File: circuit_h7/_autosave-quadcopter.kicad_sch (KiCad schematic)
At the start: 143 parts, among them J1 Conn_01x01_Female, J10 Conn_01x01_Female, J11 Conn_01x04_Male, J12 Conn_01x04_Male, J13 Conn_01x01_Female, J14 Conn_01x01_Female, J15 Conn_01x01_Female, J16 Conn_01x01_Female, J17 Conn_01x01_Female, J18 USB_C_Receptacle_USB2.0, J19 Conn_01x08_Male, J2 Conn_01x01_Female, J20 Conn_01x01_Female, J21 Conn_01x01_Female, J22 Conn_01x01_Female, J23 Conn_01x01_Female, J24 Conn_01x01_Female, J25 Conn_01x01_Female, J26 Conn_01x01_Female, J28 Conn_01x01_Female, J29 Conn_01x01_Female, J3 Conn_01x01_Female, J30 Conn_01x01_Female, J31 Conn_01x01_Female, J32 Conn_01x01_Female, J33 Conn_01x01_Female, J37 Conn_01x01_Female, J4 Conn_01x01_Female, J40 Conn_01x01_Female, J41 Conn_01x01_Female, J42 Conn_01x01_Female, J43 Conn_01x01_Female, J44 Conn_01x01_Female, J45 Conn_01x01_Female, J47 Conn_01x01_Female, J48 Conn_01x01_Female, J49 Conn_01x01_Female, J5 Conn_Coaxial, J50 Conn_01x01_Female, J6 Conn_01x06_Male, J7 Conn_01x01_Female, J8 Conn_01x01_Female, J9 Conn_01x01_Female, Q1 AO3400A, SW1 SW_DIP_x01, U1 STM32H723VGH6, U10 ESP8285, U11 AMS1117-5.0, U12 TPS5430DDA, U13 5v, 3A, U2 ICM-42605, U3 DPS310, U4 3V3, U5 EUP3458 1.2A, 30V max input, 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, U6 2450FM07D0034T, U7 W25Q80DVUXIE TR (16M), U8 SX1281, U9 5v, 500mA, Y1 16M, Y2 52Mhz, 12pF, Y3 40M

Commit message: More work on H7 board. Removed ctrl mix from firmware
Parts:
- added J27, J34, J35, J36: Conn_01x01_Female, TestPoint:TestPoint_Pad_1.0x1.0mm, symbol Connector:Conn_01x01_Female
- J12: now left out of the parts list
- J3, J31, J37: footprint TestPoint:TestPoint_Pad_1.5x1.5mm -> TestPoint:TestPoint_Pad_2.0x2.0mm
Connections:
- net GND: now also J27.1 (Pin_1); no longer J12.1 (Pin_1)
- net NRST: now also J36.1 (Pin_1); no longer J12.4 (Pin_4)
- net SWCLK: now also J35.1 (Pin_1); no longer J12.3 (Pin_3)
- net SWDIO: now also J34.1 (Pin_1); no longer J12.2 (Pin_2)
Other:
- moved on the sheet: J12
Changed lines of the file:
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@@
     (effects (font (size 1.27 1.27)) (justify left bottom))
   )
+  (label "NRST" (at 534.67 80.01 180)
+    (effects (font (size 1.27 1.27)) (justify right bottom))
+  )
   (label "M4" (at 427.99 40.64 180)
     (effects (font (size 1.27 1.27)) (justify right bottom))
@@
     (effects (font (size 1.27 1.27)) (justify left bottom))
   )
+  (label "SWDIO" (at 534.67 69.85 180)
+    (effects (font (size 1.27 1.27)) (justify right bottom))
+  )
   (label "ELRS_BUSY" (at 48.26 297.18 180)
     (effects (font (size 1.27 1.27)) (justify right bottom))
@@
     (effects (font (size 1.27 1.27)) (justify right bottom))
   )
+  (label "SWCLK" (at 534.67 74.93 180)
+    (effects (font (size 1.27 1.27)) (justify right bottom))
+  )
   (label "UART1_RX" (at 381 215.9 180)
     (effects (font (size 1.27 1.27)) (justify right bottom))
@@
     (pin "9")
   )
-  (symbol (lib_id "Connector:Conn_01x04_Male") (at 523.24 54.61 0) (unit 1)
-    (in_bom yes) (on_board yes) (fields_autoplaced)
-    (property "Reference" "J12" (id 0) (at 523.875 46.99 0))
-    (property "Value" "Conn_01x04_Male" (id 1) (at 523.875 49.53 0))
-    (property "Footprint" "Anyleaf_Shared:JST PH staggered for 1x04 2mm" (id 2) (at 523.24 54.61 0)
+  (symbol (lib_id "Connector:Conn_01x04_Male") (at 547.37 53.34 0) (unit 1)
+    (in_bom no) (on_board no) (fields_autoplaced)
+    (property "Reference" "J12" (id 0) (at 548.005 45.72 0))
+    (property "Value" "Conn_01x04_Male" (id 1) (at 548.005 48.26 0))
+    (property "Footprint" "Anyleaf_Shared:JST PH staggered for 1x04 2mm" (id 2) (at 547.37 53.34 0)
       (effects (font (size 1.27 1.27)) hide)
     )
-    (property "Datasheet" "~" (id 3) (at 523.24 54.61 0)
+    (property "Datasheet" "~" (id 3) (at 547.37 53.34 0)
       (effects (font (size 1.27 1.27)) hide)
     )
@@
     (pin "2")
   )
+  (symbol (lib_id "Connector:Conn_01x01_Female") (at 539.75 69.85 0) (unit 1)
+    (in_bom yes) (on_board yes) (fields_autoplaced)
+    (property "Reference" "J34" (id 0) (at 541.02 68.5799 0)
+      (effects (font (size 1.27 1.27)) (justify left))
+    )
+    (property "Value" "Conn_01x01_Female" (id 1) (at 541.02 71.1199 0)
+      (effects (font (size 1.27 1.27)) (justify left))
+    )
+    (property "Footprint" "TestPoint:TestPoint_Pad_1.0x1.0mm" (id 2) (at 539.75 69.85 0)
+      (effects (font (size 1.27 1.27)) hide)
+    )
+    (property "Datasheet" "~" (id 3) (at 539.75 69.85 0)
+      (effects (font (size 1.27 1.27)) hide)
+    )
+    (pin "1")
+  )
   (symbol (lib_id "Connector:Conn_01x01_Female") (at 445.77 102.87 0) (unit 1)
     (in_bom yes) (on_board yes) (fields_autoplaced)
@@
       (effects (font (size 1.27 1.27)) (justify left))
     )
-    (property "Footprint" "TestPoint:TestPoint_Pad_1.5x1.5mm" (id 2) (at 436.88 189.23 0)
+    (property "Footprint" "TestPoint:TestPoint_Pad_2.0x2.0mm" (id 2) (at 436.88 189.23 0)
       (effects (font (size 1.27 1.27)) hide)
     )
@@
       (effects (font (size 1.27 1.27)) (justify left))
     )
-    (property "Footprint" "TestPoint:TestPoint_Pad_1.5x1.5mm" (id 2) (at 436.88 193.04 0)
+    (property "Footprint" "TestPoint:TestPoint_Pad_2.0x2.0mm" (id 2) (at 436.88 193.04 0)
       (effects (font (size 1.27 1.27)) hide)
     )
@@
     (pin "2")
   )
+  (symbol (lib_id "Connector:Conn_01x01_Female") (at 539.75 64.77 0) (unit 1)
+    (in_bom yes) (on_board yes) (fields_autoplaced)
+    (property "Reference" "J27" (id 0) (at 541.02 63.4999 0)
+      (effects (font (size 1.27 1.27)) (justify left))
+    )
+    (property "Value" "Conn_01x01_Female" (id 1) (at 541.02 66.0399 0)
+      (effects (font (size 1.27 1.27)) (justify left))
+    )
+    (property "Footprint" "TestPoint:TestPoint_Pad_1.0x1.0mm" (id 2) (at 539.75 64.77 0)
+      (effects (font (size 1.27 1.27)) hide)
+    )
+    (property "Datasheet" "~" (id 3) (at 539.75 64.77 0)
+      (effects (font (size 1.27 1.27)) hide)
+    )
+    (pin "1")
+  )
   (symbol (lib_id "Device:R") (at 427.99 165.1 270) (unit 1)
     (in_bom no) (on_board no)
@@
     )
   )
+  (symbol (lib_id "Connector:Conn_01x01_Female") (at 539.75 74.93 0) (unit 1)
+    (in_bom yes) (on_board yes) (fields_autoplaced)
+    (property "Reference" "J35" (id 0) (at 541.02 73.6599 0)
+      (effects (font (size 1.27 1.27)) (justify left))
+    )
+    (property "Value" "Conn_01x01_Female" (id 1) (at 541.02 76.1999 0)
+      (effects (font (size 1.27 1.27)) (justify left))
+    )
+    (property "Footprint" "TestPoint:TestPoint_Pad_1.0x1.0mm" (id 2) (at 539.75 74.93 0)
+      (effects (font (size 1.27 1.27)) hide)
+    )
+    (property "Datasheet" "~" (id 3) (at 539.75 74.93 0)
+      (effects (font (size 1.27 1.27)) hide)
+    )
+    (pin "1")
+  )
   (symbol (lib_id "Memory_Flash:W25Q128JVS") (at 123.19 201.93 0) (unit 1)
     (in_bom yes) (on_board yes)
@@
     (pin "2")
   )
+  (symbol (lib_id "power:GND") (at 534.67 64.77 270) (unit 1)
+    (in_bom yes) (on_board yes)
+    (property "Reference" "#PWR0202" (id 0) (at 528.32 64.77 0)
+      (effects (font (size 1.27 1.27)) hide)
+    )
+    (property "Value" "GND" (id 1) (at 531.4188 64.897 90)
+      (effects (font (size 1.27 1.27)) (justify right))
+    )
+    (property "Footprint" "" (id 2) (at 534.67 64.77 0)
+      (effects (font (size 1.27 1.27)) hide)
+    )
+    (property "Datasheet" "" (id 3) (at 534.67 64.77 0)
+      (effects (font (size 1.27 1.27)) hide)
+    )
+    (pin "1")
+  )
   (symbol (lib_id "Connector:Conn_01x01_Female") (at 330.2 180.34 0) (unit 1)
     (in_bom yes) (on_board yes) (fields_autoplaced)
@@
       (effects (font (size 1.27 1.27)) (justify left))
     )
-    (property "Footprint" "TestPoint:TestPoint_Pad_1.5x1.5mm" (id 2) (at 436.88 185.42 0)
+    (property "Footprint" "TestPoint:TestPoint_Pad_2.0x2.0mm" (id 2) (at 436.88 185.42 0)
       (effects (font (size 1.27 1.27)) hide)
     )
@@
     (pin "K9")
   )
+  (symbol (lib_id "Connector:Conn_01x01_Female") (at 539.75 80.01 0) (unit 1)
+    (in_bom yes) (on_board yes) (fields_autoplaced)
+    (property "Reference" "J36" (id 0) (at 541.02 78.7399 0)
+      (effects (font (size 1.27 1.27)) (justify left))
+    )
+    (property "Value" "Conn_01x01_Female" (id 1) (at 541.02 81.2799 0)
+      (effects (font (size 1.27 1.27)) (justify left))
+    )
+    (property "Footprint" "TestPoint:TestPoint_Pad_1.0x1.0mm" (id 2) (at 539.75 80.01 0)
+      (effects (font (size 1.27 1.27)) hide)
+    )
+    (property "Datasheet" "~" (id 3) (at 539.75 80.01 0)
+      (effects (font (size 1.27 1.27)) hide)
+    )
+    (pin "1")
+  )
   (symbol (lib_id "Device:C") (at 193.04 123.19 0) (unit 1)
     (in_bom yes) (on_board yes)
@@
       (reference "#PWR0201") (unit 1) (value "GND") (footprint "")
     )
+    (path "/a289413c-0c4d-4a19-bc26-fa23e8cc885d"
+      (reference "#PWR0202") (unit 1) (value "GND") (footprint "")
+    )
     (path "/4392ec2f-3eec-47ea-978d-f1725d990b74"
       (reference "C1") (unit 1) (value "2.2u") (footprint "Capacitor_SMD:C_0402_1005Metric")
@@
     )
     (path "/c133fc7d-8123-40f5-8c56-e9e76438874b"
-      (reference "J3") (unit 1) (value "Conn_01x01_Female") (footprint "TestPoint:TestPoint_Pad_1.5x1.5mm")
+      (reference "J3") (unit 1) (value "Conn_01x01_Female") (footprint "TestPoint:TestPoint_Pad_2.0x2.0mm")
     )
     (path "/9a634a5d-301b-4e5d-8af1-f867e3dc6295"
@@
       (reference "J26") (unit 1) (value "Conn_01x01_Female") (footprint "TestPoint:TestPoint_Pad_2.0x2.0mm")
     )
+    (path "/7fba9677-1bdf-4eec-ba59-c15db75e2803"
+      (reference "J27") (unit 1) (value "Conn_01x01_Female") (footprint "TestPoint:TestPoint_Pad_1.0x1.0mm")
+    )
     (path "/7eb8e8c3-0828-4397-860b-9862e2e588bc"
       (reference "J28") (unit 1) (value "Conn_01x01_Female") (footprint "TestPoint:TestPoint_Pad_2.0x2.0mm")
@@
     )
     (path "/6f306190-2ba5-496c-b7f5-7797a51aa9fc"
-      (reference "J31") (unit 1) (value "Conn_01x01_Female") (footprint "TestPoint:TestPoint_Pad_1.5x1.5mm")
+      (reference "J31") (unit 1) (value "Conn_01x01_Female") (footprint "TestPoint:TestPoint_Pad_2.0x2.0mm")
     )
     (path "/c911782e-07fe-4168-af65-34d646808183"
@@
       (reference "J33") (unit 1) (value "Conn_01x01_Female") (footprint "TestPoint:TestPoint_Pad_2.0x2.0mm")
     )
+    (path "/1bae9465-2fd4-4482-9fea-8a1dd644ef6f"
+      (reference "J34") (unit 1) (value "Conn_01x01_Female") (footprint "TestPoint:TestPoint_Pad_1.0x1.0mm")
+    )
+    (path "/8c9b0052-026d-4d73-a5b3-b412fa6ead30"
+      (reference "J35") (unit 1) (value "Conn_01x01_Female") (footprint "TestPoint:TestPoint_Pad_1.0x1.0mm")
+    )
+    (path "/f310b3ef-d915-470f-9cc3-1761ccea4ad4"
+      (reference "J36") (unit 1) (value "Conn_01x01_Female") (footprint "TestPoint:TestPoint_Pad_1.0x1.0mm")
+    )
     (path "/2a2364df-a1c0-4811-a54e-02a9d0ea9408"
-      (reference "J37") (unit 1) (value "Conn_01x01_Female") (footprint "TestPoint:TestPoint_Pad_1.5x1.5mm")
+      (reference "J37") (unit 1) (value "Conn_01x01_Female") (footprint "TestPoint:TestPoint_Pad_2.0x2.0mm")
     )
     (path "/0567dae1-cf2c-438a-99dc-8576c8bfdd09"

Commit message: More work on H7 board
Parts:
- removed C21: 10nF 50V, Capacitor_SMD:C_0402_1005Metric, symbol Device:C
- removed C22: 2.2u, Capacitor_SMD:C_0402_1005Metric, symbol Device:C
- removed C24: 47uF 16V, Capacitor_SMD:C_1210_3225Metric, symbol Device:C
- removed C27: 22u 35v, Capacitor_SMD:C_0805_2012Metric, symbol Device:C
- removed C42: 150p, Capacitor_SMD:C_0402_1005Metric, symbol Device:C
- removed C43: 100n, Capacitor_SMD:C_0402_1005Metric, symbol Device:C
- removed C44: 1.5n, Capacitor_SMD:C_0402_1005Metric, symbol Device:C
- removed C45, C46: 10u, Capacitor_SMD:C_0805_2012Metric, symbol Device:C
- removed D2: 40v 1A B5819WS, Diode_SMD:D_SOD-323, symbol Device:D
- removed L4: 22u 900mA, Anyleaf_Shared:SMNR4020 inductor, symbol Device:L
- removed R17: 300, Resistor_SMD:R_0402_1005Metric, symbol Device:R
- removed R19: 10k, Resistor_SMD:R_0402_1005Metric, symbol Device:R
- removed U11: AMS1117-5.0, Package_TO_SOT_SMD:SOT-223-3_TabPin2, symbol Regulator_Linear:AMS1117-5.0
- removed U13: 5v, 3A, Package_DFN_QFN:DFN-10-1EP_3x3mm_P0.5mm_EP1.65x2.38mm, symbol water_monitor-rescue:MCP1802-3.3-Anyleaf_shared
- removed U5: EUP3458 1.2A, 30V max input, adj output, Package_TO_SOT_SMD:TSOT-23-6, symbol Regulator_Switching:AAT1217ICA-1.2
- removed U9: 5v, 500mA, Package_TO_SOT_SMD:TSOT-23-5, symbol water_monitor-rescue:MCP1802-3.3-Anyleaf_shared
- added J38, J39: Conn_01x01_Female, TestPoint:TestPoint_Pad_1.0x1.0mm, symbol Connector:Conn_01x01_Female
- added U5: MT2492 600kHz 16v 2A, Package_TO_SOT_SMD:SOT-23-6, symbol Regulator_Switching:TPS5430DDA
- C14: value 10uF 50V -> 22uF 25v; LCSC C440198 -> C602037; now in the parts list
- C15: value 1u 50V -> 22n; footprint Capacitor_SMD:C_0603_1608Metric -> Capacitor_SMD:C_0402_1005Metric; LCSC C15849 -> C1532; now in the parts list
- C20: value 47uF 16V -> 100uF 6.3V; footprint Capacitor_SMD:C_1210_3225Metric -> Capacitor_SMD:C_1206_3216Metric; LCSC C412625 -> C15008; now in the parts list
- L2: value 100u 450mA -> 10u 2A; footprint Anyleaf_Shared:SMNR4020 inductor -> Inductor_SMD:L_Taiyo-Yuden_MD-4040; LCSC C467068 -> C98364; now in the parts list
- R10: value 3.3K -> 1.4k; LCSC C25890 -> C39650
- R11: value 300 -> 13k; footprint Resistor_SMD:R_0402_1005Metric -> Resistor_SMD:R_0603_1608Metric; LCSC C25102 -> C22797
- R7: value 3.3K -> 10k; LCSC C25890 -> C25744; now in the parts list
- R8: value 300 -> 100k; LCSC C25102 -> C25741; now in the parts list
- U12: value TPS5430DDA -> TPS5430DDA 3A 36v
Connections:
- net +10V: now also C14.2, U5.1 (BS), U5.3 (FB); no longer C20.1
- net +BATT: no longer C14.2
- net GND: now also J39.1 (Pin_1); no longer C15.1, R8.1
- net ELRS_BOOT: now reaches U10.15 (GPIO0)
- net ELRS_BOOT: now also J38.1 (Pin_1)
- net ELRS_LED: now reaches R9.2, U10.8 (XPD_DCDC)
- net at U12.4 (VSENSE): now also R10.2, R7.1; no longer R11.2
- net at D5.2 (A): now also C20.1, L2.2, R8.2
- net at L2.1: now also C15.2
- new net: R11.2, R8.1, U5.4 (EN)
- new net: C15.1, U5.5 (VIN)
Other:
- note added: "10v - 5v regulator"
- note added: "See DS for info on selecting passives (5v reg)"
- note added: "These passives (for the 10v reg)chosen based on an official interactive TI tool. Screenshot of results included in folder."
- note added: "battery - 10v regulator"
- note added: "todo: Consider 1-2 10uF caps here (1206 likely)"
- note added: "todo: Is a 1A diode here good enough?"
- note added: "todo: consider 22uH here"
- note removed: "3.3k and 300 lead to 9.6V output"
- note removed: "Calculated inductor value, for 25.2v in, 9.6vout, 30% ripple, and 1A current: 16.5uH"
- note removed: "Todo: 1A may not be enough. 2A should be"
- note removed: "Todo: Sort out passives on this 5v reg"
- note removed: "V_out = 0.8V * (R1 + R2)/R2"
- note removed: "extended part. Basic v is 1206"
- note removed: "todo: Find part for this 10ju cap"
- note removed: "todo: Non-extended part for this 1.5n cap?"
- moved on the sheet: C38, C39, C40, C41, D7, H1, H2, H3, H4, L5, R10, U12

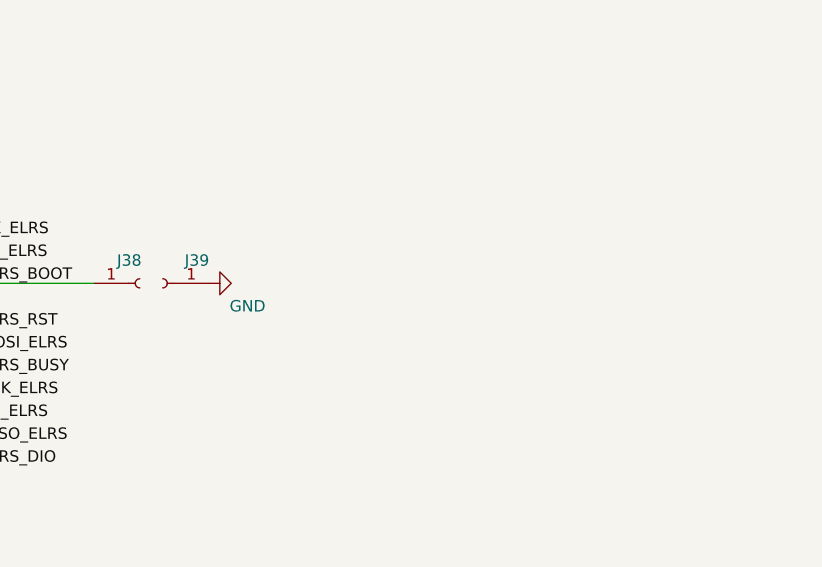
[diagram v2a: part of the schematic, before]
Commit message: Started to revamp gyro and imu interp with att platform to fix errors and be consistent. Moved some code out of IMU drivers to imu_shared, or delted
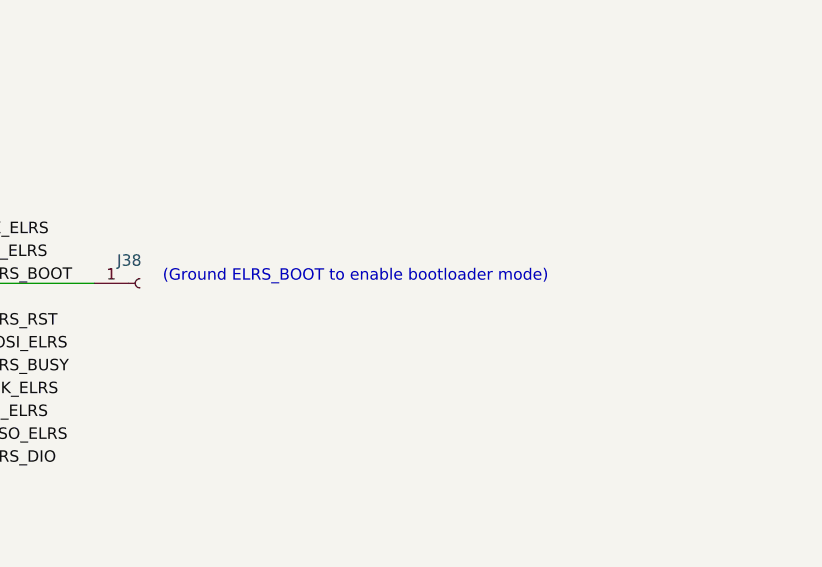
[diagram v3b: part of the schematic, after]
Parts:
- removed J39: Conn_01x01_Female, TestPoint:TestPoint_Pad_1.0x1.0mm, symbol Connector:Conn_01x01_Female
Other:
- note added: "(Ground ELRS_BOOT to enable bootloader mode)"
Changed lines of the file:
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@@
     (effects (font (size 1.27 1.27)) (justify left bottom))
   )
+  (text "(Ground ELRS_BOOT to enable bootloader mode)" (at 457.2 330.2 0)
+    (effects (font (size 1.27 1.27)) (justify left bottom))
+  )
   (text "24-52Mhz crystal" (at 372.11 354.33 0)
     (effects (font (size 1.27 1.27)) (justify left bottom))
@@
     (pin "4")
   )
-  (symbol (lib_id "power:GND") (at 462.28 330.2 90) (unit 1)
-    (in_bom yes) (on_board yes)
-    (property "Reference" "#PWR0158" (id 0) (at 468.63 330.2 0)
-      (effects (font (size 1.27 1.27)) hide)
-    )
-    (property "Value" "GND" (id 1) (at 468.63 332.74 90)
-      (effects (font (size 1.27 1.27)) (justify left))
-    )
-    (property "Footprint" "" (id 2) (at 462.28 330.2 0)
-      (effects (font (size 1.27 1.27)) hide)
-    )
-    (property "Datasheet" "" (id 3) (at 462.28 330.2 0)
-      (effects (font (size 1.27 1.27)) hide)
-    )
-    (pin "1")
-  )
   (symbol (lib_id "Connector:Conn_01x08_Male") (at 478.79 53.34 180) (unit 1)
     (in_bom yes) (on_board yes)
@@
     (pin "1")
   )
-  (symbol (lib_id "Connector:Conn_01x01_Female") (at 457.2 330.2 180) (unit 1)
-    (in_bom no) (on_board yes)
-    (property "Reference" "J39" (id 0) (at 461.01 327.66 0))
-    (property "Value" "Conn_01x01_Female" (id 1) (at 457.835 327.66 0)
-      (effects (font (size 1.27 1.27)) hide)
-    )
-    (property "Footprint" "TestPoint:TestPoint_Pad_1.0x1.0mm" (id 2) (at 457.2 330.2 0)
-      (effects (font (size 1.27 1.27)) hide)
-    )
-    (property "Datasheet" "~" (id 3) (at 457.2 330.2 0)
-      (effects (font (size 1.27 1.27)) hide)
-    )
-    (pin "1")
-  )
   (symbol (lib_id "power:GND") (at 193.04 119.38 180) (unit 1)
     (in_bom yes) (on_board yes) (fields_autoplaced)
@@
       (reference "#PWR0157") (unit 1) (value "GND") (footprint "")
     )
-    (path "/b98995ac-4e84-46ec-b29a-bcb09545e600"
-      (reference "#PWR0158") (unit 1) (value "GND") (footprint "")
-    )
     (path "/6e50da88-c872-42c7-9b4e-194a13623160"
       (reference "#PWR0160") (unit 1) (value "GND") (footprint "")
@@
       (reference "J38") (unit 1) (value "Conn_01x01_Female") (footprint "TestPoint:TestPoint_Pad_1.0x1.0mm")
     )
-    (path "/ba99e4c2-0c03-4c8d-b4a3-70560b5a25fe"
-      (reference "J39") (unit 1) (value "Conn_01x01_Female") (footprint "TestPoint:TestPoint_Pad_1.0x1.0mm")
-    )
     (path "/0567dae1-cf2c-438a-99dc-8576c8bfdd09"
